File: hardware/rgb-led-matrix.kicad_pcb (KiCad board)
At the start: 2 copper layers, 17.5 x 25 mm, 19 parts, among them P1 CON-SENSOR, Q1 2N7002P, U1 M24C64, U2 DRILL, U3 DRILL, U4 DRILL, U5 DRILL

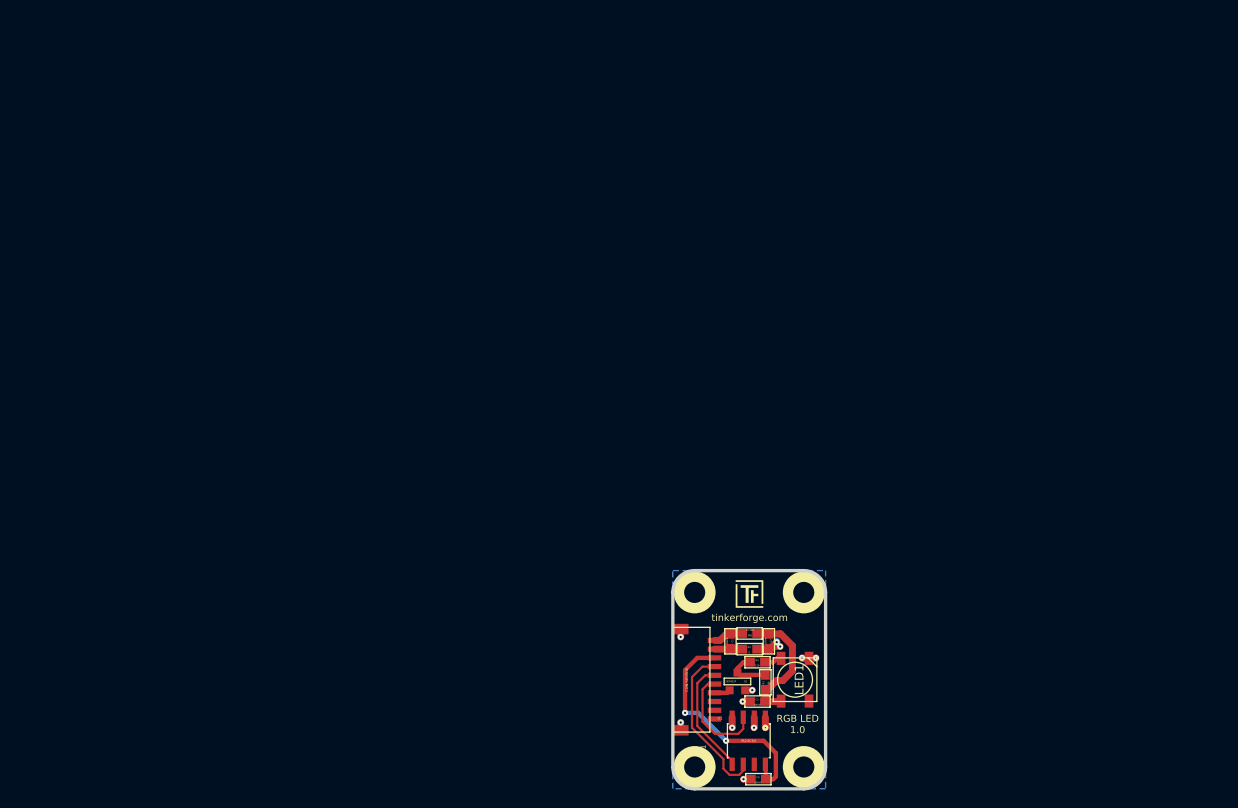
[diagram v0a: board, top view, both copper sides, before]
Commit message: leds not fully placed and routed
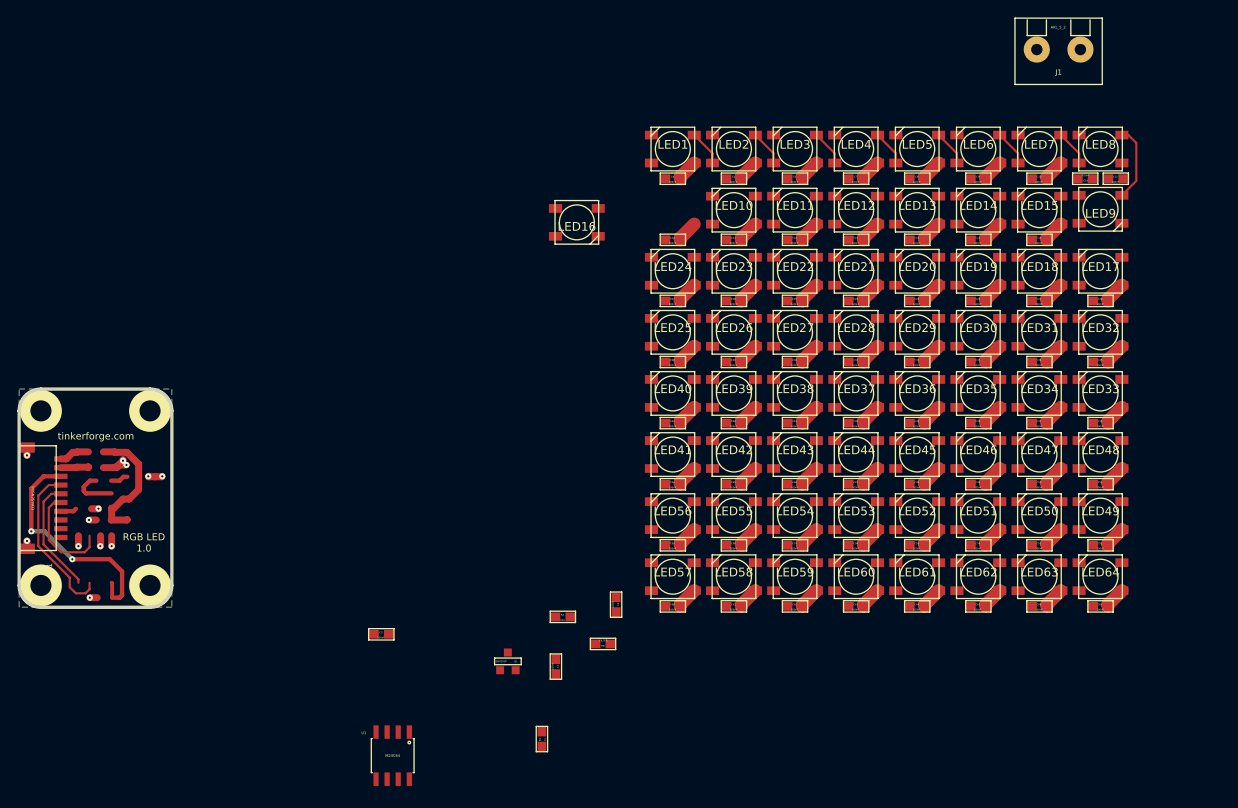
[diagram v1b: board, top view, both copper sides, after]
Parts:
- removed G***: Logo_31x31, kicad-libraries:Logo_31x31
- removed G***: LOGO, kicad-libraries:WEEE_7mm
- removed R3: 330, kicad-libraries:0603E
- removed VAL: CE_5mm, kicad-libraries:CE_5mm
- added C10: 100nF, kicad-libraries:0603E, F.Cu at (167.3, 60.7)
- added C11: 100nF, kicad-libraries:0603E, F.Cu at (176.1, 60.7)
- added C12: 100nF, kicad-libraries:0603E, F.Cu at (125.3, 67.7)
- added C13: 100nF, kicad-libraries:0603E, F.Cu at (132.3, 67.7)
- added C14: 100nF, kicad-libraries:0603E, F.Cu at (139.3, 67.7)
- added C15: 100nF, kicad-libraries:0603E, F.Cu at (146.3, 67.7)
- added C16: 100nF, kicad-libraries:0603E, F.Cu at (153.3, 67.7)
- added C17: 100nF, kicad-libraries:0603E, F.Cu at (160.3, 67.7)
- added C18: 100nF, kicad-libraries:0603E, F.Cu at (167.3, 67.7)
- added C19: 100nF, kicad-libraries:0603E, F.Cu at (172.6, 60.7)
- added C20: 100nF, kicad-libraries:0603E, F.Cu at (174.3, 74.7)
- added C21: 100nF, kicad-libraries:0603E, F.Cu at (167.3, 74.7)
- added C22: 100nF, kicad-libraries:0603E, F.Cu at (160.3, 74.7)
- added C23: 100nF, kicad-libraries:0603E, F.Cu at (153.3, 74.7)
- added C24: 100nF, kicad-libraries:0603E, F.Cu at (146.3, 74.7)
- added C25: 100nF, kicad-libraries:0603E, F.Cu at (139.3, 74.7)
- added C26: 100nF, kicad-libraries:0603E, F.Cu at (132.3, 74.7)
- added C27: 100nF, kicad-libraries:0603E, F.Cu at (125.3, 74.7)
- added C28: 100nF, kicad-libraries:0603E, F.Cu at (125.3, 81.7)
- added C29: 100nF, kicad-libraries:0603E, F.Cu at (132.3, 81.7)
- added C30: 100nF, kicad-libraries:0603E, F.Cu at (139.3, 81.7)
- added C31: 100nF, kicad-libraries:0603E, F.Cu at (146.3, 81.7)
- added C32: 100nF, kicad-libraries:0603E, F.Cu at (153.3, 81.7)
- added C33: 100nF, kicad-libraries:0603E, F.Cu at (160.3, 81.7)
- added C34: 100nF, kicad-libraries:0603E, F.Cu at (167.3, 81.7)
- added C35: 100nF, kicad-libraries:0603E, F.Cu at (174.3, 81.7)
- added C36: 100nF, kicad-libraries:0603E, F.Cu at (174.3, 88.7)
- added C37: 100nF, kicad-libraries:0603E, F.Cu at (167.3, 88.7)
- added C38: 100nF, kicad-libraries:0603E, F.Cu at (160.3, 88.7)
- added C39: 100nF, kicad-libraries:0603E, F.Cu at (153.3, 88.7)
- added C40: 100nF, kicad-libraries:0603E, F.Cu at (146.3, 88.7)
- added C41: 100nF, kicad-libraries:0603E, F.Cu at (139.3, 88.7)
- added C42: 100nF, kicad-libraries:0603E, F.Cu at (132.3, 88.7)
- added C43: 100nF, kicad-libraries:0603E, F.Cu at (125.3, 88.7)
- added C44: 100nF, kicad-libraries:0603E, F.Cu at (125.3, 95.7)
- added C45: 100nF, kicad-libraries:0603E, F.Cu at (132.3, 95.7)
- added C46: 100nF, kicad-libraries:0603E, F.Cu at (139.3, 95.7)
- added C47: 100nF, kicad-libraries:0603E, F.Cu at (146.3, 95.7)
- added C48: 100nF, kicad-libraries:0603E, F.Cu at (153.3, 95.7)
- added C49: 100nF, kicad-libraries:0603E, F.Cu at (160.3, 95.7)
- added C5: 100nF, kicad-libraries:0603E, F.Cu at (132.3, 60.7)
- added C50: 100nF, kicad-libraries:0603E, F.Cu at (167.3, 95.7)
- added C51: 100nF, kicad-libraries:0603E, F.Cu at (174.3, 95.7)
- added C52: 100nF, kicad-libraries:0603E, F.Cu at (174.3, 102.7)
- added C53: 100nF, kicad-libraries:0603E, F.Cu at (167.3, 102.7)
- added C54: 100nF, kicad-libraries:0603E, F.Cu at (160.3, 102.7)
- added C55: 100nF, kicad-libraries:0603E, F.Cu at (153.3, 102.7)
- added C56: 100nF, kicad-libraries:0603E, F.Cu at (146.3, 102.7)
- added C57: 100nF, kicad-libraries:0603E, F.Cu at (139.3, 102.7)
- added C58: 100nF, kicad-libraries:0603E, F.Cu at (132.3, 102.7)
- added C59: 100nF, kicad-libraries:0603E, F.Cu at (125.3, 102.7)
- added C6: 100nF, kicad-libraries:0603E, F.Cu at (139.3, 60.7)
- added C60: 100nF, kicad-libraries:0603E, F.Cu at (125.3, 109.7)
- added C61: 100nF, kicad-libraries:0603E, F.Cu at (132.3, 109.7)
- added C62: 100nF, kicad-libraries:0603E, F.Cu at (139.3, 109.7)
- added C63: 100nF, kicad-libraries:0603E, F.Cu at (146.3, 109.7)
- added C64: 100nF, kicad-libraries:0603E, F.Cu at (153.3, 109.7)
- added C65: 100nF, kicad-libraries:0603E, F.Cu at (160.3, 109.7)
- added C66: 100nF, kicad-libraries:0603E, F.Cu at (167.3, 109.7)
- added C67: 100nF, kicad-libraries:0603E, F.Cu at (174.3, 109.7)
- added C7: 100nF, kicad-libraries:0603E, F.Cu at (146.3, 60.7)
- added C8: 100nF, kicad-libraries:0603E, F.Cu at (153.3, 60.7)
- added C9: 100nF, kicad-libraries:0603E, F.Cu at (160.3, 60.7)
- added J1: AKL_5_2, kicad-libraries:AKL_5_2, F.Cu at (169.5, 45.9)
- added LED10: WS2812B_LED, kicad-libraries:WS2812B_LED, F.Cu at (132.3, 64.3)
- added LED11: WS2812B_LED, kicad-libraries:WS2812B_LED, F.Cu at (139.3, 64.3)
- added LED12: WS2812B_LED, kicad-libraries:WS2812B_LED, F.Cu at (146.3, 64.3)
- added LED13: WS2812B_LED, kicad-libraries:WS2812B_LED, F.Cu at (153.3, 64.3)
- added LED14: WS2812B_LED, kicad-libraries:WS2812B_LED, F.Cu at (160.3, 64.3)
- added LED15: WS2812B_LED, kicad-libraries:WS2812B_LED, F.Cu at (167.3, 64.3)
- added LED16: WS2812B_LED, kicad-libraries:WS2812B_LED, F.Cu at (114.3, 65.7)
- added LED17: WS2812B_LED, kicad-libraries:WS2812B_LED, F.Cu at (174.3, 71.3)
- added LED18: WS2812B_LED, kicad-libraries:WS2812B_LED, F.Cu at (167.3, 71.3)
- added LED19: WS2812B_LED, kicad-libraries:WS2812B_LED, F.Cu at (160.3, 71.3)
- added LED2: WS2812B_LED, kicad-libraries:WS2812B_LED, F.Cu at (132.3, 57.3)
- added LED20: WS2812B_LED, kicad-libraries:WS2812B_LED, F.Cu at (153.3, 71.3)
- added LED21: WS2812B_LED, kicad-libraries:WS2812B_LED, F.Cu at (146.3, 71.3)
- added LED22: WS2812B_LED, kicad-libraries:WS2812B_LED, F.Cu at (139.3, 71.3)
- added LED23: WS2812B_LED, kicad-libraries:WS2812B_LED, F.Cu at (132.3, 71.3)
- added LED24: WS2812B_LED, kicad-libraries:WS2812B_LED, F.Cu at (125.3, 71.3)
- added LED25: WS2812B_LED, kicad-libraries:WS2812B_LED, F.Cu at (125.3, 78.3)
- added LED26: WS2812B_LED, kicad-libraries:WS2812B_LED, F.Cu at (132.3, 78.3)
- added LED27: WS2812B_LED, kicad-libraries:WS2812B_LED, F.Cu at (139.3, 78.3)
- added LED28: WS2812B_LED, kicad-libraries:WS2812B_LED, F.Cu at (146.3, 78.3)
- added LED29: WS2812B_LED, kicad-libraries:WS2812B_LED, F.Cu at (153.3, 78.3)
- added LED3: WS2812B_LED, kicad-libraries:WS2812B_LED, F.Cu at (139.3, 57.3)
- added LED30: WS2812B_LED, kicad-libraries:WS2812B_LED, F.Cu at (160.3, 78.3)
- added LED31: WS2812B_LED, kicad-libraries:WS2812B_LED, F.Cu at (167.3, 78.3)
- added LED32: WS2812B_LED, kicad-libraries:WS2812B_LED, F.Cu at (174.3, 78.3)
- added LED33: WS2812B_LED, kicad-libraries:WS2812B_LED, F.Cu at (174.3, 85.3)
- added LED34: WS2812B_LED, kicad-libraries:WS2812B_LED, F.Cu at (167.3, 85.3)
- added LED35: WS2812B_LED, kicad-libraries:WS2812B_LED, F.Cu at (160.3, 85.3)
- added LED36: WS2812B_LED, kicad-libraries:WS2812B_LED, F.Cu at (153.3, 85.3)
- added LED37: WS2812B_LED, kicad-libraries:WS2812B_LED, F.Cu at (146.3, 85.3)
- added LED38: WS2812B_LED, kicad-libraries:WS2812B_LED, F.Cu at (139.3, 85.3)
- added LED39: WS2812B_LED, kicad-libraries:WS2812B_LED, F.Cu at (132.3, 85.3)
- added LED4: WS2812B_LED, kicad-libraries:WS2812B_LED, F.Cu at (146.3, 57.3)
- added LED40: WS2812B_LED, kicad-libraries:WS2812B_LED, F.Cu at (125.3, 85.3)
- added LED41: WS2812B_LED, kicad-libraries:WS2812B_LED, F.Cu at (125.3, 92.3)
- added LED42: WS2812B_LED, kicad-libraries:WS2812B_LED, F.Cu at (132.3, 92.3)
- added LED43: WS2812B_LED, kicad-libraries:WS2812B_LED, F.Cu at (139.3, 92.3)
- added LED44: WS2812B_LED, kicad-libraries:WS2812B_LED, F.Cu at (146.3, 92.3)
- added LED45: WS2812B_LED, kicad-libraries:WS2812B_LED, F.Cu at (153.3, 92.3)
- added LED46: WS2812B_LED, kicad-libraries:WS2812B_LED, F.Cu at (160.3, 92.3)
- added LED47: WS2812B_LED, kicad-libraries:WS2812B_LED, F.Cu at (167.3, 92.3)
- added LED48: WS2812B_LED, kicad-libraries:WS2812B_LED, F.Cu at (174.3, 92.3)
- added LED49: WS2812B_LED, kicad-libraries:WS2812B_LED, F.Cu at (174.3, 99.3)
- added LED5: WS2812B_LED, kicad-libraries:WS2812B_LED, F.Cu at (153.3, 57.3)
- added LED50: WS2812B_LED, kicad-libraries:WS2812B_LED, F.Cu at (167.3, 99.3)
- added LED51: WS2812B_LED, kicad-libraries:WS2812B_LED, F.Cu at (160.3, 99.3)
- added LED52: WS2812B_LED, kicad-libraries:WS2812B_LED, F.Cu at (153.3, 99.3)
- added LED53: WS2812B_LED, kicad-libraries:WS2812B_LED, F.Cu at (146.3, 99.3)
- added LED54: WS2812B_LED, kicad-libraries:WS2812B_LED, F.Cu at (139.3, 99.3)
- added LED55: WS2812B_LED, kicad-libraries:WS2812B_LED, F.Cu at (132.3, 99.3)
- added LED56: WS2812B_LED, kicad-libraries:WS2812B_LED, F.Cu at (125.3, 99.3)
- added LED57: WS2812B_LED, kicad-libraries:WS2812B_LED, F.Cu at (125.3, 106.3)
- added LED58: WS2812B_LED, kicad-libraries:WS2812B_LED, F.Cu at (132.3, 106.3)
- added LED59: WS2812B_LED, kicad-libraries:WS2812B_LED, F.Cu at (139.3, 106.3)
- added LED6: WS2812B_LED, kicad-libraries:WS2812B_LED, F.Cu at (160.3, 57.3)
- added LED60: WS2812B_LED, kicad-libraries:WS2812B_LED, F.Cu at (146.3, 106.3)
- added LED61: WS2812B_LED, kicad-libraries:WS2812B_LED, F.Cu at (153.3, 106.3)
- added LED62: WS2812B_LED, kicad-libraries:WS2812B_LED, F.Cu at (160.3, 106.3)
- added LED63: WS2812B_LED, kicad-libraries:WS2812B_LED, F.Cu at (167.3, 106.3)
- added LED64: WS2812B_LED, kicad-libraries:WS2812B_LED, F.Cu at (174.3, 106.3)
- added LED7: WS2812B_LED, kicad-libraries:WS2812B_LED, F.Cu at (167.3, 57.3)
- added LED8: WS2812B_LED, kicad-libraries:WS2812B_LED, F.Cu at (174.3, 57.3)
- added LED9: WS2812B_LED, kicad-libraries:WS2812B_LED, F.Cu at (174.3, 64.2)
- R2: value 0 -> 330
- moved P1 77.7 mm to (50.4, 97.3)
- moved U2 77.7 mm to (52.9, 87.3)
- moved U3 77.7 mm to (65.4, 107.3)
- moved U4 77.7 mm to (52.9, 107.3)
- moved U5 77.7 mm to (65.4, 87.3)
- moved C4 69.5 mm to (125.3, 60.7)
- moved LED1 62.4 mm to (125.3, 57.3), turned to 180 degrees
- moved C3 43.8 mm to (91.9, 112.9)
- moved U1 40.8 mm to (93.2, 126.8)
- moved R1 26.4 mm to (110.3, 124.9)
- moved Q1 26.4 mm to (106.4, 116.0)
- moved R2 21.7 mm to (112.7, 110.9)
- moved C1 20.2 mm to (111.9, 116.6)
- moved C2 18.0 mm to (118.8, 109.5)
- moved FB1 16.8 mm to (117.3, 114.0)
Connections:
- C1 pad 1: Net-(C1-Pad1) -> GND
- C1 pad 2: Net-(C1-Pad2) -> VCC
- C2 pad 2: VCC -> Net-(C2-Pad2)
- C3 pad 1: VCC -> 3V3
- C4 pad 1: 3V3 -> VCC
- FB1 pad 1: Net-(C1-Pad2) -> Net-(C2-Pad2)
- LED1 pad 2: (no net) -> Net-(LED1-Pad2)
- P1 pad 1: Net-(C1-Pad2) -> (no net)
- P1 pad 2: Net-(C1-Pad1) -> GND
- R2 pad 1: GND -> Net-(LED1-Pad4)
- R2 pad 2: Net-(C1-Pad1) -> Net-(Q1-PadD)
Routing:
- net VCC: track 14.8 -> 152.7 mm
- net (no net): track 0.00 -> 37.7 mm, vias 0 -> 10
- net Net-(LED8-Pad2): track 0.00 -> 8.71 mm
- net GND: track 13.6 -> 5.09 mm, vias 12 -> 2
- net Net-(Q1-PadD): track 5.53 -> 0.00 mm
- net Net-(LED7-Pad2): track 0.00 -> 4.07 mm
- net Net-(LED6-Pad2): track 0.00 -> 4.07 mm
- net Net-(LED5-Pad2): track 0.00 -> 4.07 mm
- net Net-(LED4-Pad2): track 0.00 -> 4.07 mm
- net Net-(LED3-Pad2): track 0.00 -> 4.07 mm
- net Net-(LED2-Pad2): track 0.00 -> 4.07 mm
- net Net-(LED1-Pad2): track 0.00 -> 4.07 mm
- net Net-(C1-Pad2): track 3.51 -> 0.00 mm
- net Net-(C1-Pad1): track 3.29 -> 0.00 mm
- net Net-(LED1-Pad4): track 2.04 -> 0.00 mm

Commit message: fully routed
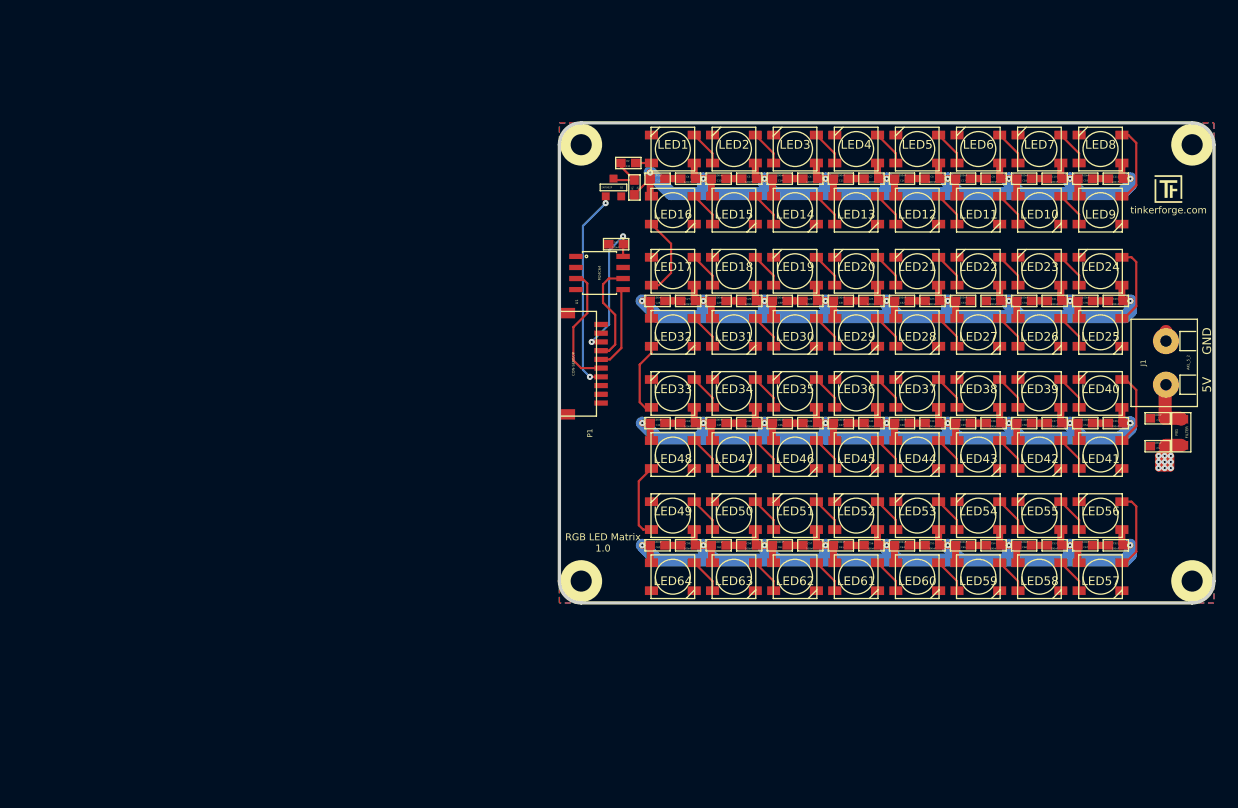
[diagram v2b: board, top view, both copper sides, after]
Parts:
- added G***: Logo_31x31, kicad-libraries:Logo_31x31, F.Cu at (180.5, 60.3)
- added VAL: WEEE_7mm_back, kicad-libraries:WEEE_7mm_back, B.Cu at (146.3, 81.9)
- added VAL: CE_5mm, kicad-libraries:CE_5mm, B.Cu at (153.3, 81.9)
- FB1: footprint kicad-libraries:0603E -> kicad-libraries:1206
- moved U2 133.3 mm to (184.8, 106.8)
- moved U3 129.6 mm to (184.8, 56.8)
- moved U4 79.9 mm to (114.8, 56.8)
- moved C1 73.4 mm to (180.8, 91.3), turned to 0 degrees
- moved FB1 70.5 mm to (183.6, 89.8), turned to 270 degrees
- moved C2 65.6 mm to (180.8, 88.2), turned to 0 degrees
- moved R1 64.1 mm to (120.9, 61.7)
- moved P1 63.8 mm to (112.3, 81.9)
- moved U1 60.2 mm to (116.9, 71.5), turned to 270 degrees
- moved Q1 55.6 mm to (118.5, 61.7)
- moved U5 53.1 mm to (114.8, 106.8)
- moved R2 52.5 mm to (120.2, 58.9)
- moved C3 52.2 mm to (118.8, 68.2)
- moved LED17 49.0 mm to (125.3, 71.3)
- moved LED24 49.0 mm to (174.3, 71.3)
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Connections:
- J1 pad 1: Net-(C2-Pad2) -> GND
- J1 pad 2: GND -> Net-(C2-Pad2)
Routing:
- net VCC: track 152.7 -> 489.3 mm, vias 0 -> 46
- net GND: track 5.09 -> 56.9 mm, vias 2 -> 0
- net (no net): track 37.7 -> 0.00 mm, vias 10 -> 0
- net Net-(P1-Pad7): track 1.85 -> 23.4 mm, vias 0 -> 2
- net Net-(LED16-Pad2): track 0.00 -> 10.3 mm
- net 3V3: track 26.9 -> 17.0 mm
- net Net-(LED32-Pad2): track 0.00 -> 9.56 mm
- net Net-(LED56-Pad2): track 0.00 -> 9.41 mm
- net Net-(LED24-Pad2): track 0.00 -> 9.23 mm
- net Net-(LED48-Pad2): track 0.00 -> 9.21 mm
- net Net-(LED40-Pad2): track 0.00 -> 8.63 mm
- net SCL: track 18.6 -> 12.0 mm
- net Net-(C2-Pad2): track 0.00 -> 5.78 mm
- net Net-(Q1-PadD): track 0.00 -> 5.06 mm
- net Net-(LED63-Pad2): track 0.00 -> 4.07 mm
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- added copper zone on F.Cu, net GND
- added copper zone on B.Cu, net VCC
- removed copper zone on B.Cu, net GND
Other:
- board size 17.5 x 25 mm -> 75 x 55 mm
- board text added: "5V"
- board text added: "GND"
- board text added: "RGB LED Matrix 1.0"
- board text removed: "RGB LED 1.0"

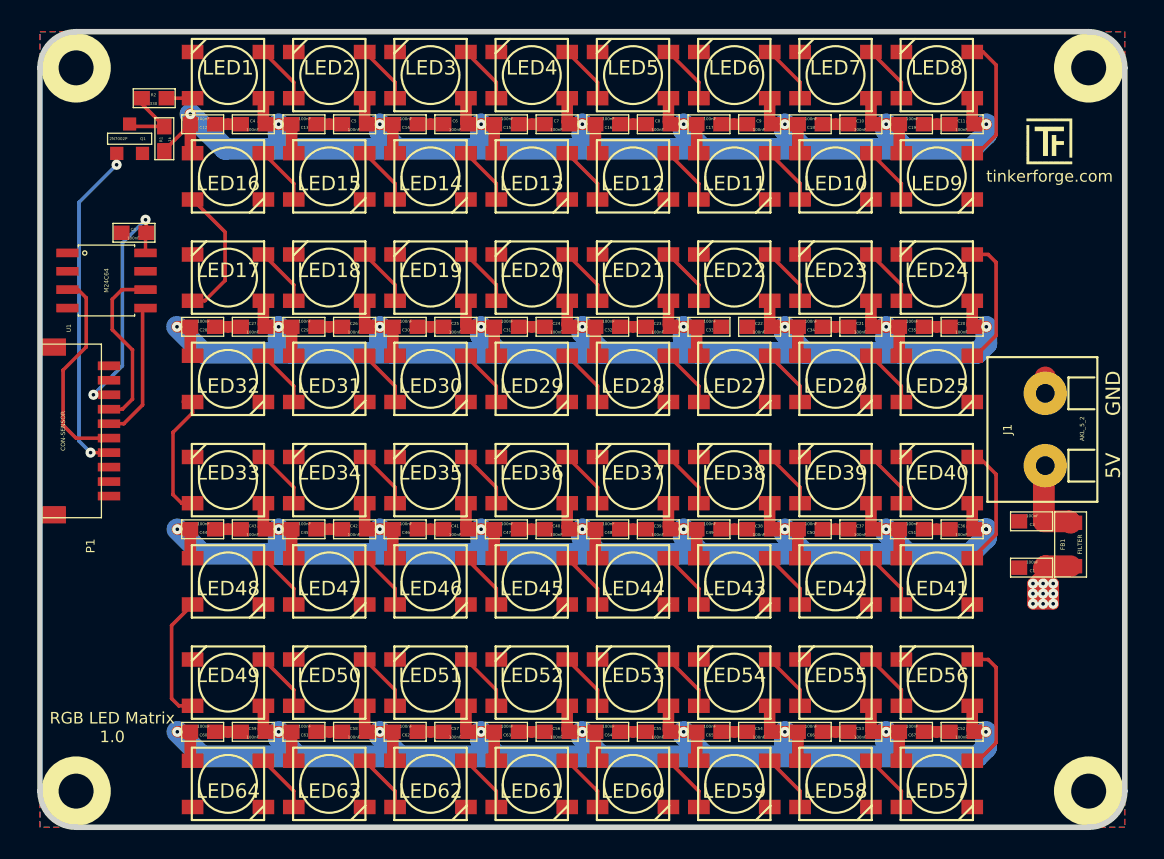
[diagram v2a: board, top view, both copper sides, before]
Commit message: add xmc1100 microcontroller
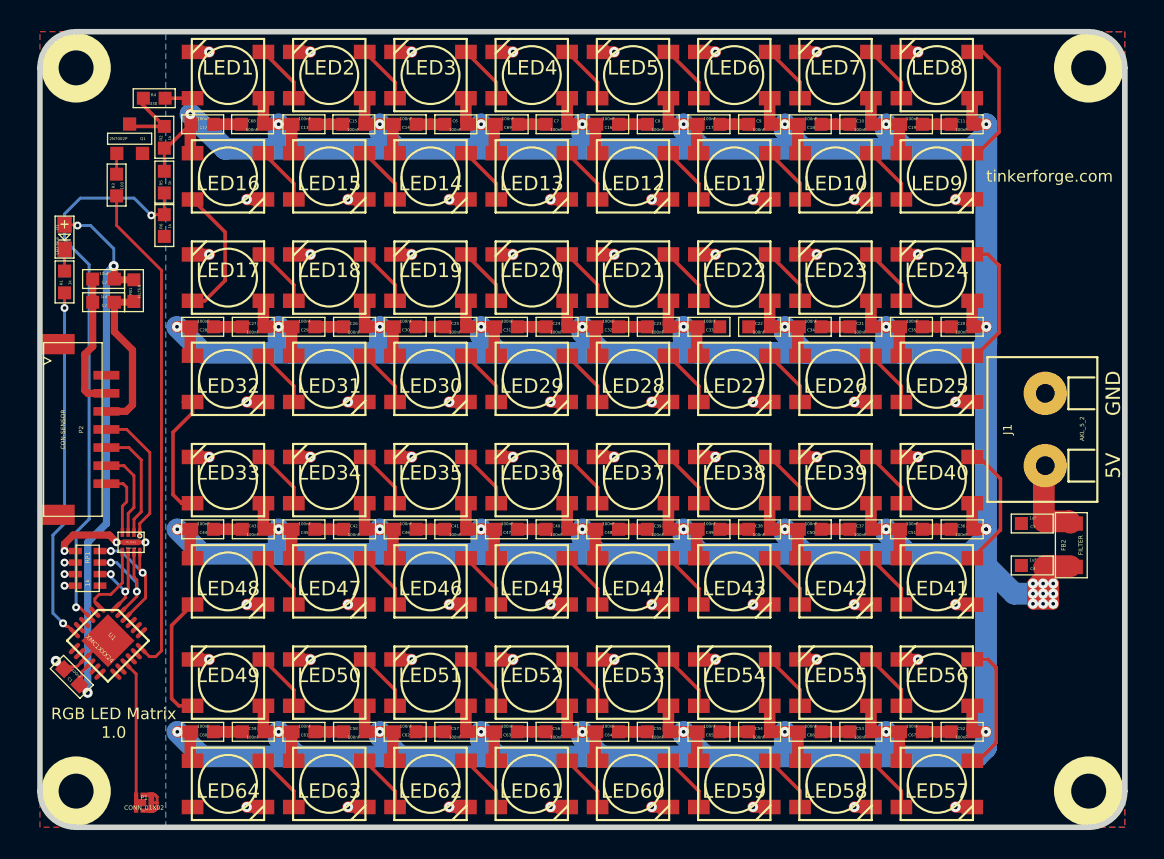
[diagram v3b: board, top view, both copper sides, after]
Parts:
- removed G***: Logo_31x31, kicad-libraries:Logo_31x31
- removed VAL: WEEE_7mm_back, kicad-libraries:WEEE_7mm_back
- removed VAL: CE_5mm, kicad-libraries:CE_5mm
- added C68: 100nF, kicad-libraries:0603F, F.Cu at (127.0, 60.7)
- added C69: 100nF, kicad-libraries:0603F, F.Cu at (144.6, 60.7)
- added D1: LED blue, kicad-libraries:D0603E, F.Cu at (114.0, 68.5)
- added FB2: FILTER, kicad-libraries:1206, F.Cu at (183.6, 89.8)
- added FILTER1: Filter-4x, kicad-libraries:DFN8-17x135, F.Cu at (118.6, 89.6)
- added P2: CON-SENSOR, kicad-libraries:CON-SENSOR2, F.Cu at (112.3, 81.8)
- added R3: 100, kicad-libraries:0603F, F.Cu at (117.6, 64.9)
- added R4: 330, kicad-libraries:0603F, F.Cu at (120.2, 58.9)
- added R5: 1k, kicad-libraries:0603F, F.Cu at (120.9, 64.7)
- added R6: 1k, kicad-libraries:0603F, F.Cu at (120.9, 67.7)
- added RP1: 1k, 0603X4, F.Cu at (115.6, 91.4)
- C1, C10, C11, C12, C13, C14, C15, C16, C17, C18, C19, C20, C21, C22, C23, C24, C25, C26, C27, C28, C29, C30, C31, C32, C33, C34, C35, C36, C37, C38, C39, C40, C41, C42, C43, C44, C45, C46, C47, C48, C49, C50, C51, C52, C53, C54, C55, C56, C57, C58, C59, C6, C60, C61, C62, C63, C64, C65, C66, C67, C7, C8, C9, R1: footprint kicad-libraries:0603E -> kicad-libraries:0603F
- C2, C4, C5: value 100nF -> 1uF; footprint kicad-libraries:0603E -> kicad-libraries:0603F
- C3: value 100nF -> 10uF; footprint kicad-libraries:0603E -> kicad-libraries:0603F
- FB1: footprint kicad-libraries:1206 -> kicad-libraries:0603F
- P1: value CON-SENSOR -> CONN_01X02; footprint kicad-libraries:CON-SENSOR -> kicad-libraries:SolderJumper
- R2: value 330 -> 1k; footprint kicad-libraries:0603E -> kicad-libraries:0603F
- U1: value M24C64 -> XMC1XXX24; footprint kicad-libraries:SOIC8 -> kicad-libraries:QFN24-4x4mm-0.5mm
- moved FB1 67.1 mm to (118.8, 72.2)
- moved C1 66.8 mm to (114.5, 98.9), turned to 315 degrees
- moved C2 65.9 mm to (116.7, 73.0)
- moved C4 61.9 mm to (180.9, 91.2), turned to 0 degrees
- moved C5 54.4 mm to (180.9, 88.3), turned to 0 degrees
- moved P1 26.7 mm to (119.5, 107.6), turned to 180 degrees
- moved U1 24.9 mm to (117.0, 96.4), turned to 315 degrees
- moved R1 12.1 mm to (114.0, 71.6)
- moved C15 10.6 mm to (134.0, 60.7), turned to 180 degrees
- moved C3 3.83 mm to (116.7, 71.4), turned to 0 degrees
- moved R2 2.79 mm to (120.9, 61.6), turned to 270 degrees
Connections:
- C1 pad 2: VCC -> 3V3
- C3 pad 1: 3V3 -> GND
- C3 pad 2: GND -> 3V3
- C4 pad 1: VCC -> GND
- C4 pad 2: GND -> VCC
- C5 pad 1: VCC -> GND
- C5 pad 2: GND -> Net-(C5-Pad2)
- FB1 pad 1: Net-(C2-Pad2) -> 3V3
- FB1 pad 2: VCC -> Net-(C2-Pad2)
- J1 pad 2: Net-(C2-Pad2) -> Net-(C5-Pad2)
- P1 pad 1: (no net) -> GND
- P1 pad 2: GND -> Net-(P1-Pad2)
- Q1 pad G: Net-(P1-Pad7) -> Net-(Q1-PadG)
- R1 pad 1: Net-(Q1-PadD) -> Net-(D1-Pad2)
- R1 pad 2: VCC -> Net-(R1-Pad2)
- R2 pad 1: Net-(LED1-Pad4) -> Net-(Q1-PadD)
- R2 pad 2: Net-(Q1-PadD) -> VCC
- U1 pad 1: GND -> S-MISO
- U1 pad 2: GND -> (no net)
- U1 pad 3: Net-(P1-Pad6) -> VIN
- U1 pad 4: GND -> (no net)
- U1 pad 5: SDA -> (no net)
- U1 pad 6: SCL -> Net-(R1-Pad2)
- U1 pad 8: 3V3 -> (no net)
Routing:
- net GND: track 56.9 -> 160.4 mm, vias 0 -> 71
- net VCC: track 489.3 -> 537.6 mm
- net VIN: track 0.00 -> 38.9 mm, vias 0 -> 2
- net Net-(R3-Pad2): track 0.00 -> 34.5 mm
- net Net-(R1-Pad2): track 0.00 -> 24.5 mm, vias 0 -> 2
- net Net-(P1-Pad7): track 23.4 -> 0.00 mm, vias 2 -> 0
- net 3V3: track 17.0 -> 40.3 mm, vias 2 -> 3
- net Net-(P1-Pad6): track 14.5 -> 0.00 mm
- net SCL: track 12.0 -> 0.00 mm
- net Net-(P1-Pad2): track 0.00 -> 10.3 mm
- net SDA: track 9.64 -> 0.00 mm
- net Net-(FILTER1-Pad1): track 0.00 -> 9.48 mm
- net S-CS: track 0.00 -> 8.81 mm, vias 0 -> 2
- net S-CLK: track 0.00 -> 8.43 mm, vias 0 -> 2
- net Net-(FILTER1-Pad2): track 0.00 -> 7.98 mm
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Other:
- net class Default: clearance 0.14986 -> 0.15; trace_width 0.249 -> 0.2; via_dia 0.70104 -> 0.55; via_drill 0.24892 -> 0.25
- rule trace_clearance: 0.14986 -> 0.15
- rule trace_min: 0.249 -> 0.2
- rule via_min_drill: 0.24892 -> 0.25
- rule via_min_size: 0.70104 -> 0.5
